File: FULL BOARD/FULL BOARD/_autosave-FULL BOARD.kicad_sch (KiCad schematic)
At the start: 101 parts, among them IC1 TAS5760LDAP, J1 PJ-036AH-SMT-TR, J2 Micro_SD_Card, J3 B2B-PH-K-S, J4 5019514000, J5 61201021621, J6 B2B-PH-K-S, SW1 PTS645SK50SMTR92LFS, U1 LD1117S33TR_SOT223, U2 STM32H743VITx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

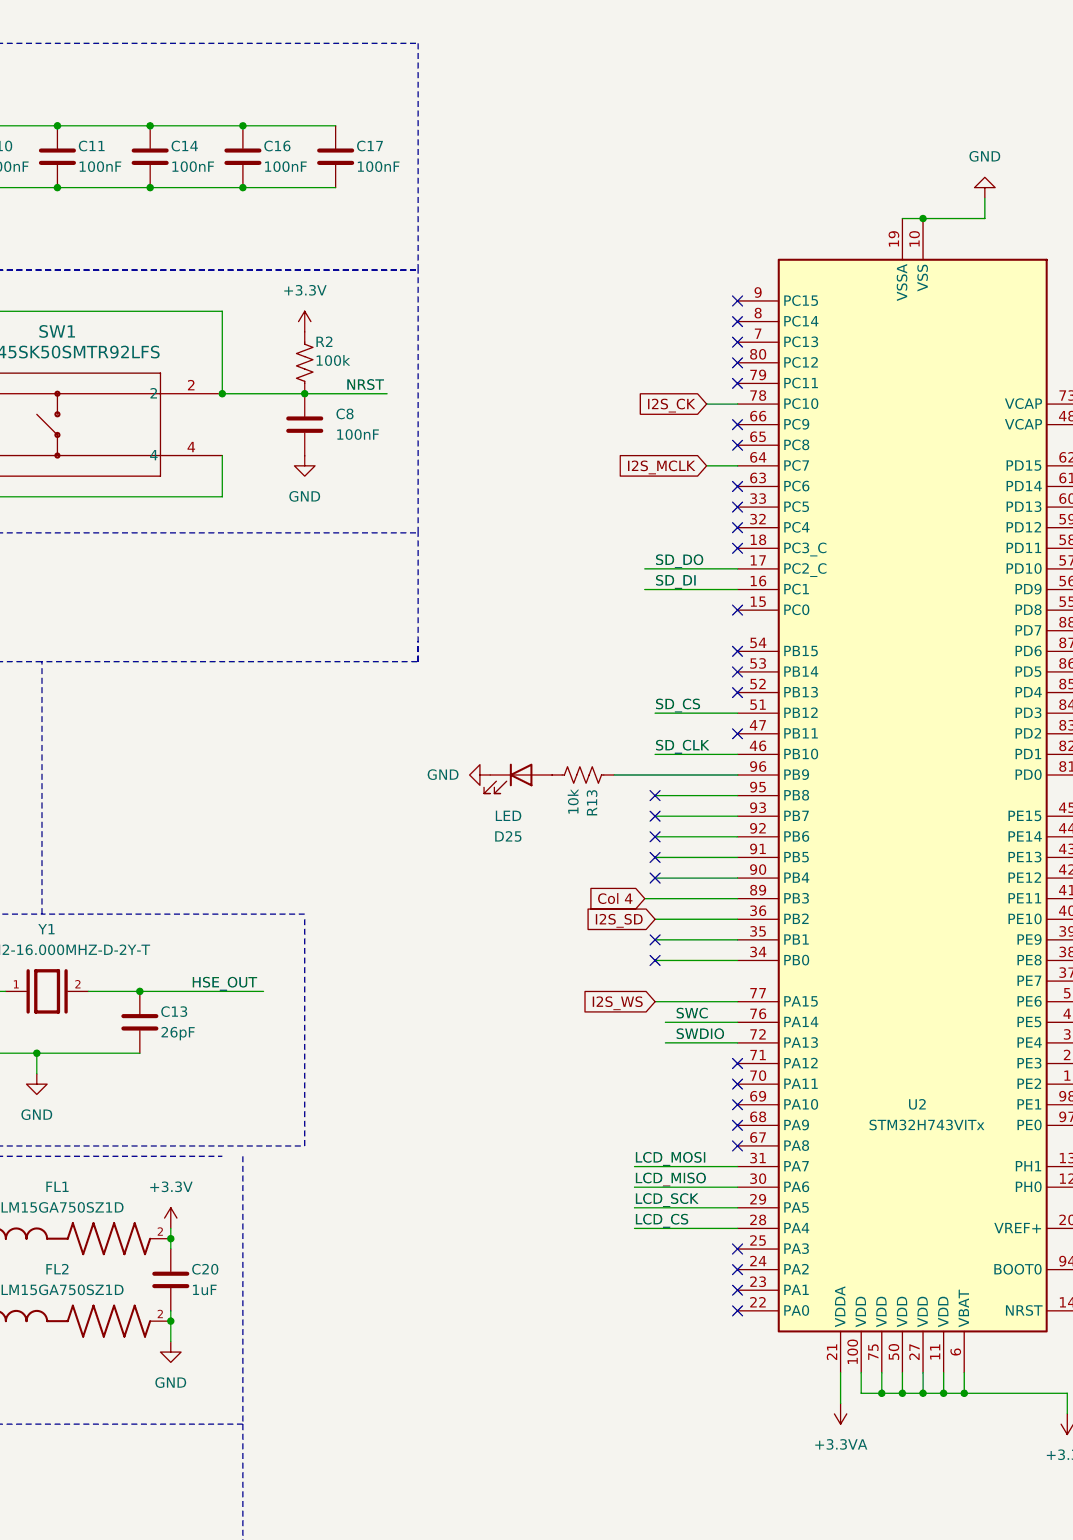
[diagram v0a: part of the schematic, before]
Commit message: changed LCD footprint, GNDA
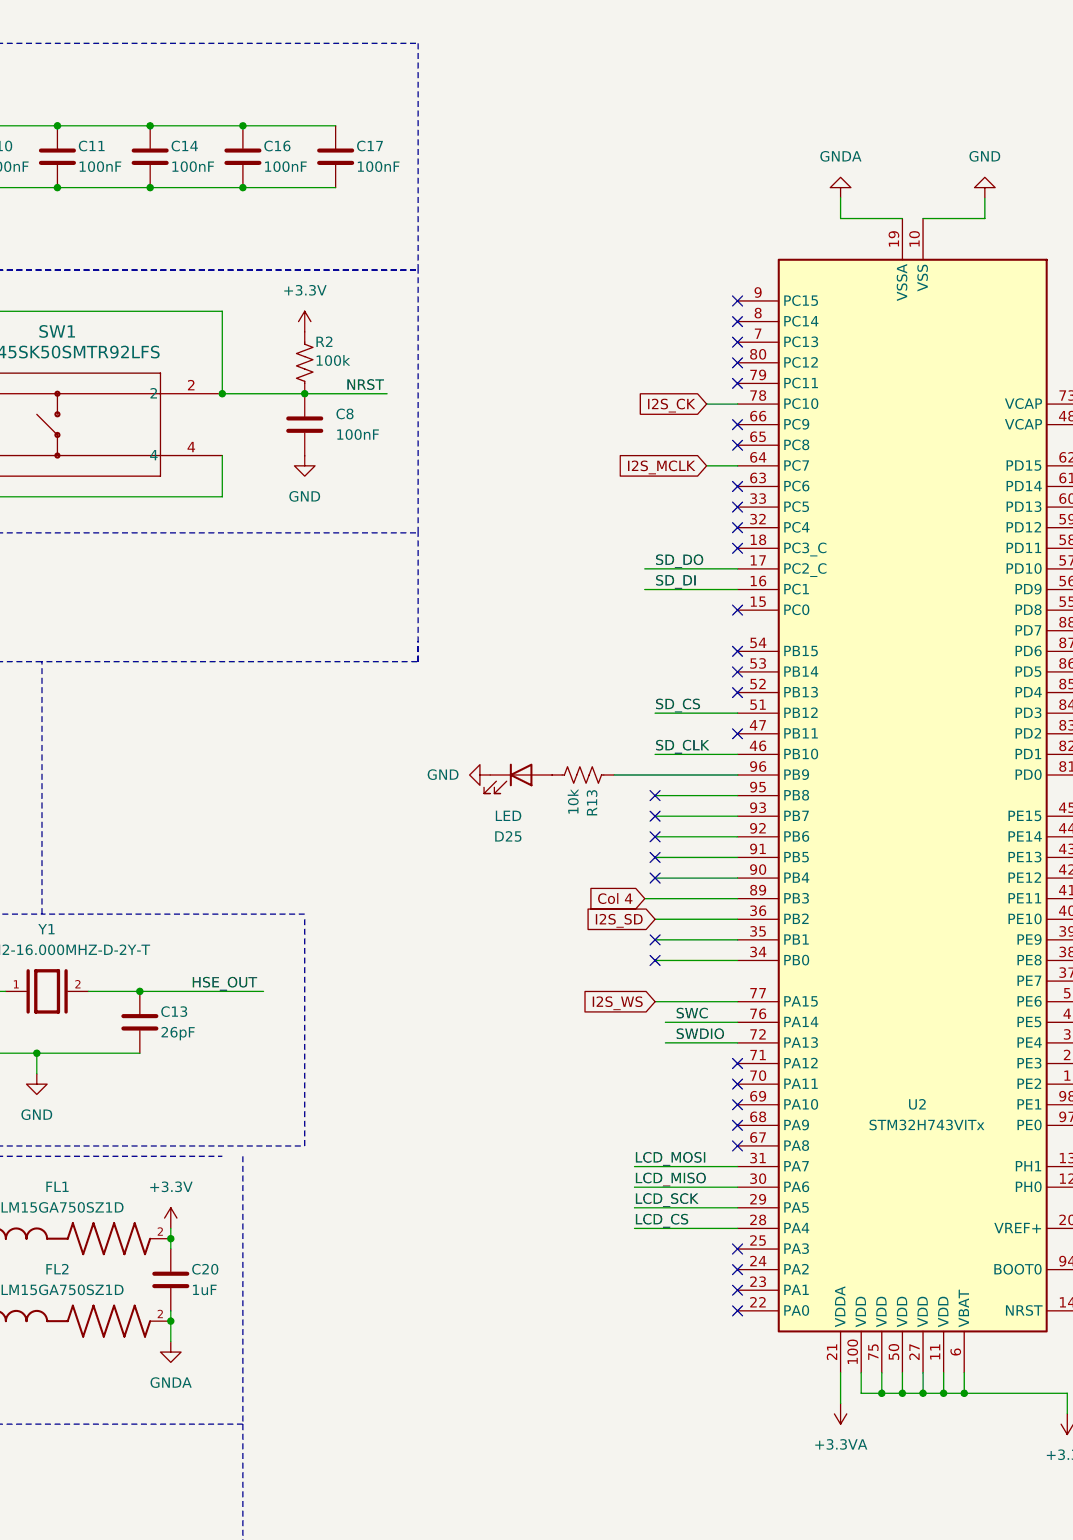
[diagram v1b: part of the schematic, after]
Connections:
- net GND: no longer C20.2, FL2.2, U2.19 (VSSA)
- new net GNDA: C20.2, FL2.2, U2.19 (VSSA)
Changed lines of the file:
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@@
 	)
 	(junction
-		(at 161.29 120.65)
-		(diameter 0)
-		(color 0 0 0 0)
-	)
-	(junction
 		(at 163.83 265.43)
 		(diameter 0)
@@
 	(wire
 		(pts
+			(xy 158.75 120.65) (xy 151.13 120.65)
+		)
+		(stroke
+			(width 0)
+			(type default)
+		)
+	)
+	(wire
+		(pts
 			(xy 34.29 149.86) (xy 20.32 149.86)
 		)
@@
 	(wire
 		(pts
-			(xy 161.29 120.65) (xy 158.75 120.65)
-		)
-		(stroke
-			(width 0)
-			(type default)
-		)
-	)
-	(wire
-		(pts
 			(xy 36.83 223.52) (xy 52.07 223.52)
 		)
@@
 	(wire
 		(pts
+			(xy 151.13 120.65) (xy 151.13 118.11)
+		)
+		(stroke
+			(width 0)
+			(type default)
+		)
+	)
+	(wire
+		(pts
 			(xy 392.43 182.88) (xy 405.13 182.88)
 		)
@@
 	)
 	(symbol
-		(lib_id "power:GND")
-		(at 68.58 259.08 0)
-		(unit 1)
-		(exclude_from_sim no)
-		(in_bom yes)
-		(on_board yes)
-		(dnp no)
-		(fields_autoplaced yes)
-		(property "Reference" "#PWR021"
-			(at 68.58 265.43 0)
-			(effects
-				(font
-					(size 1.27 1.27)
-				)
-				(hide yes)
-			)
-		)
-		(property "Value" "GND"
-			(at 68.58 264.16 0)
-			(effects
-				(font
-					(size 1.27 1.27)
-				)
-			)
-		)
-		(property "Footprint" ""
-			(at 68.58 259.08 0)
-			(effects
-				(font
-					(size 1.27 1.27)
-				)
-				(hide yes)
-			)
-		)
-		(property "Datasheet" ""
-			(at 68.58 259.08 0)
-			(effects
-				(font
-					(size 1.27 1.27)
-				)
-				(hide yes)
-			)
-		)
-		(property "Description" "Power symbol creates a global label with name \"GND\" , ground"
-			(at 68.58 259.08 0)
-			(effects
-				(font
-					(size 1.27 1.27)
-				)
-				(hide yes)
-			)
-		)
-		(pin "1"
-		)
-		(instances
-			(project "FULL BOARD"
-				(path "/df550598-5349-47af-a3f3-2a2a958bedd4"
-					(reference "#PWR021")
-					(unit 1)
-				)
-			)
-		)
-	)
-	(symbol
 		(lib_id "B2B-PH-K-S:B2B-PH-K-S")
 		(at 387.35 321.31 0)
@@
 	)
 	(symbol
+		(lib_id "power:GND")
+		(at 68.58 259.08 0)
+		(unit 1)
+		(exclude_from_sim no)
+		(in_bom yes)
+		(on_board yes)
+		(dnp no)
+		(fields_autoplaced yes)
+		(property "Reference" "#PWR053"
+			(at 68.58 265.43 0)
+			(effects
+				(font
+					(size 1.27 1.27)
+				)
+				(hide yes)
+			)
+		)
+		(property "Value" "GNDA"
+			(at 68.58 264.16 0)
+			(effects
+				(font
+					(size 1.27 1.27)
+				)
+			)
+		)
+		(property "Footprint" ""
+			(at 68.58 259.08 0)
+			(effects
+				(font
+					(size 1.27 1.27)
+				)
+				(hide yes)
+			)
+		)
+		(property "Datasheet" ""
+			(at 68.58 259.08 0)
+			(effects
+				(font
+					(size 1.27 1.27)
+				)
+				(hide yes)
+			)
+		)
+		(property "Description" "Power symbol creates a global label with name \"GND\" , ground"
+			(at 68.58 259.08 0)
+			(effects
+				(font
+					(size 1.27 1.27)
+				)
+				(hide yes)
+			)
+		)
+		(pin "1"
+		)
+		(instances
+			(project "FULL BOARD"
+				(path "/df550598-5349-47af-a3f3-2a2a958bedd4"
+					(reference "#PWR053")
+					(unit 1)
+				)
+			)
+		)
+	)
+	(symbol
 		(lib_name "+3.3V_2")
 		(lib_id "power:+3.3V")
@@
 					(unit 1)
 				)
+			)
+		)
+	)
+	(symbol
+		(lib_id "power:GND")
+		(at 151.13 118.11 180)
+		(unit 1)
+		(exclude_from_sim no)
+		(in_bom yes)
+		(on_board yes)
+		(dnp no)
+		(fields_autoplaced yes)
+		(property "Reference" "#PWR052"
+			(at 151.13 111.76 0)
+			(effects
+				(font
+					(size 1.27 1.27)
+				)
+				(hide yes)
+			)
+		)
+		(property "Value" "GNDA"
+			(at 151.13 113.03 0)
+			(effects
+				(font
+					(size 1.27 1.27)
+				)
+			)
+		)
+		(property "Footprint" ""
+			(at 151.13 118.11 0)
+			(effects
+				(font
+					(size 1.27 1.27)
+				)
+				(hide yes)
+			)
+		)
+		(property "Datasheet" ""
+			(at 151.13 118.11 0)
+			(effects
+				(font
+					(size 1.27 1.27)
+				)
+				(hide yes)
+			)
+		)
+		(property "Description" "Power symbol creates a global label with name \"GND\" , ground"
+			(at 151.13 118.11 0)
+			(effects
+				(font
+					(size 1.27 1.27)
+				)
+				(hide yes)
+			)
+		)
+		(pin "1"
+		)
+		(instances
+			(project "FULL BOARD"
+				(path "/df550598-5349-47af-a3f3-2a2a958bedd4"
+					(reference "#PWR052")
+					(unit 1)
+				)
